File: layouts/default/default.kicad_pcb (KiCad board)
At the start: 2 copper layers, 37 x 37 mm, 107 parts

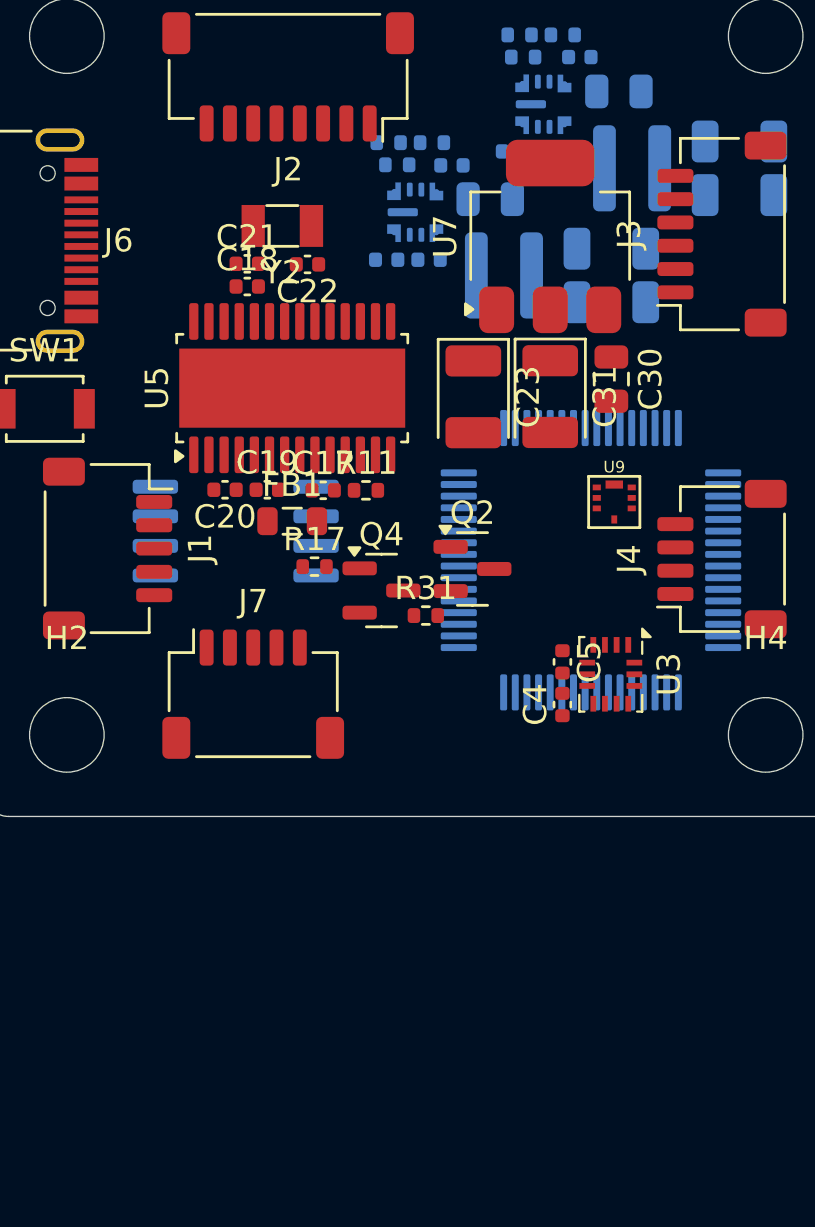
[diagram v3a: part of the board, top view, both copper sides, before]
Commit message: Replace AMS1117 with TI TLV75533 LDO, SS34 with SS54 Schottky
AMS1117 is Chinese (AMS, Shenzhen) — not NDAA compliant. TLV75533
is TI (SOT-23-5, 500mA, stable with MLCC). EN tied to VIN. SS54
is a drop-in 5A upgrade over SS34 (same SMA footprint). Both match
Brave F7 reference board components.

Co-Authored-By: Claude Opus 4.6 <noreply@anthropic.com>
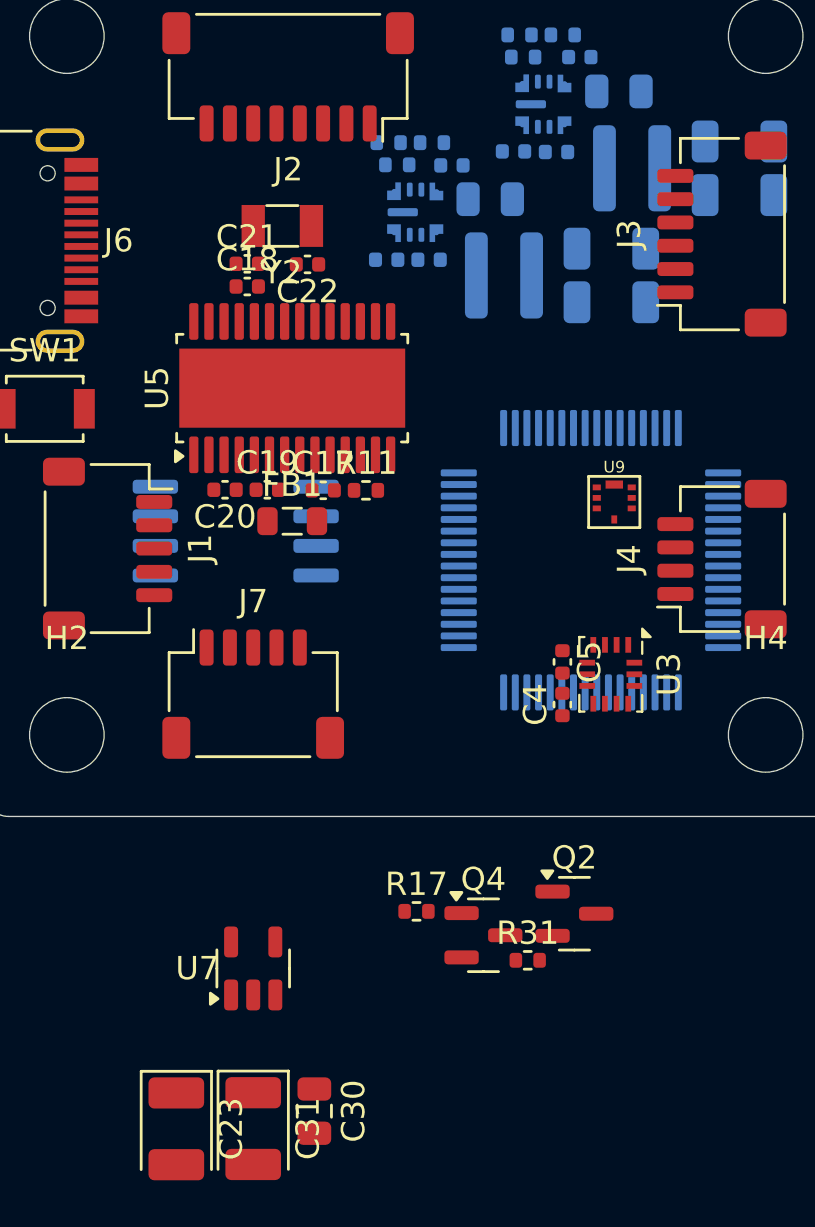
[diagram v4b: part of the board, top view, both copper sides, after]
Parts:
- U7: footprint Package_TO_SOT_SMD:SOT-223-3_TabPin2 -> Package_TO_SOT_SMD:SOT-23-5
- moved C30 33.9 mm to (114.1, 149.7)
- moved C31 33.9 mm to (111.5, 150.4)
- moved U7 33.9 mm to (111.5, 143.5)
- moved C23 33.9 mm to (108.2, 150.4)
- moved Q2 15.4 mm to (125.3, 141.2)
- moved R31 15.4 mm to (123.3, 143.2)
- moved Q4 15.4 mm to (121.4, 142.1)
- moved R17 15.4 mm to (118.5, 141.1)
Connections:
- U7 pad 1: baro-gnd -> v5
- U7 pad 2: vdd -> baro-gnd
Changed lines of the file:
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@@
     (footprint "Capacitor_Tantalum_SMD:CP_EIA-3528-21_Kemet-B"
         (layer "F.Cu")
-        (at 120.95 118.985 -90)
+        (at 108.2 150.41 -90)
         (property "Reference" "C23"
             (at 0 -2.35 90)
@@
     (footprint "Capacitor_SMD:C_0805_2012Metric"
         (layer "F.Cu")
-        (at 126.875 118.225 -90)
+        (at 114.125 149.65 -90)
         (property "Reference" "C30"
             (at 0 -1.68 90)
@@
     (footprint "Resistor_SMD:R_0402_1005Metric"
         (layer "F.Cu")
-        (at 118.91 128.375 0)
+        (at 123.285 143.175 0)
         (property "Reference" "R31"
             (at 0 -1.17 0)
@@
     (footprint "Package_TO_SOT_SMD:SOT-23"
         (layer "F.Cu")
-        (at 120.9125 126.375 0)
+        (at 125.2875 141.175 0)
         (property "Reference" "Q2"
             (at 0 -2.4 0)
@@
         )
     )
-    (footprint "Package_TO_SOT_SMD:SOT-223-3_TabPin2"
+    (footprint "Package_TO_SOT_SMD:SOT-23-5"
         (layer "F.Cu")
-        (at 124.25 112.1 90)
+        (at 111.5 143.525 90)
         (property "Reference" "U7"
-            (at 0 -4.5 90)
+            (at 0 -2.4 0)
             (layer "F.SilkS")
             (effects
@@
         )
         (property "Value" ""
-            (at 0 4.5 90)
+            (at 0 2.4 0)
             (layer "F.Fab")
             (hide no)
@@
             )
         )
-        (property "__atopile_lib_fp_hash__" "a6ccbecc-0be9-e1c9-66fc-8e409d184be7"
-            (at 0 0 90)
+        (property "__atopile_lib_fp_hash__" "1547344e-d8e7-4a11-2d2b-a920ed1ea8dd"
+            (at 0 0 0)
             (layer "User.9")
             (hide yes)
@@
         (attr smd)
         (fp_line
-            (start 1.91 -3.41)
-            (end 1.91 -2.15)
+            (start 0 -1.56)
+            (end -0.8 -1.56)
             (stroke
                 (width 0.12)
@@
         )
         (fp_line
-            (start -1.85 -3.41)
-            (end 1.91 -3.41)
+            (start 0 -1.56)
+            (end 0.8 -1.56)
             (stroke
                 (width 0.12)
@@
         )
         (fp_line
-            (start 1.91 3.41)
-            (end 1.91 2.15)
+            (start 0 1.56)
+            (end -0.8 1.56)
             (stroke
                 (width 0.12)
@@
         )
         (fp_line
-            (start -1.85 3.41)
-            (end 1.91 3.41)
+            (start 0 1.56)
+            (end 0.8 1.56)
             (stroke
                 (width 0.12)
@@
         )
         (fp_line
-            (start 4.4 -3.6)
-            (end -4.4 -3.6)
+            (start -2.05 -1.5)
+            (end -1.05 -1.5)
             (stroke
                 (width 0.05)
@@
         )
         (fp_line
-            (start -4.4 -3.6)
-            (end -4.4 3.6)
+            (start -2.05 1.5)
+            (end -2.05 -1.5)
             (stroke
                 (width 0.05)
@@
         )
         (fp_line
-            (start 4.4 3.6)
-            (end 4.4 -3.6)
+            (start -1.05 -1.7)
+            (end 1.05 -1.7)
             (stroke
                 (width 0.05)
@@
         )
         (fp_line
-            (start -4.4 3.6)
-            (end 4.4 3.6)
+            (start -1.05 -1.5)
+            (end -1.05 -1.7)
             (stroke
                 (width 0.05)
@@
         )
         (fp_line
-            (start 1.85 -3.35)
-            (end 1.85 3.35)
+            (start -1.05 1.5)
+            (end -2.05 1.5)
             (stroke
-                (width 0.1)
+                (width 0.05)
                 (type solid)
             )
-            (layer "F.Fab")
+            (layer "F.CrtYd")
         )
         (fp_line
-            (start -0.85 -3.35)
-            (end 1.85 -3.35)
+            (start -1.05 1.7)
+            (end -1.05 1.5)
             (stroke
-                (width 0.1)
+                (width 0.05)
                 (type solid)
             )
-            (layer "F.Fab")
+            (layer "F.CrtYd")
         )
         (fp_line
-            (start -1.85 -2.35)
-            (end -0.85 -3.35)
+            (start 1.05 -1.7)
+            (end 1.05 -1.5)
             (stroke
-                (width 0.1)
+                (width 0.05)
                 (type solid)
             )
-            (layer "F.Fab")
+            (layer "F.CrtYd")
         )
         (fp_line
-            (start -1.85 -2.35)
-            (end -1.85 3.35)
+            (start 1.05 -1.5)
+            (end 2.05 -1.5)
             (stroke
-                (width 0.1)
+                (width 0.05)
                 (type solid)
             )
-            (layer "F.Fab")
+            (layer "F.CrtYd")
+        )
+        (fp_line
+            (start 1.05 1.5)
+            (end 1.05 1.7)
+            (stroke
+                (width 0.05)
+                (type solid)
+            )
+            (layer "F.CrtYd")
         )
         (fp_line
-            (start -1.85 3.35)
-            (end 1.85 3.35)
+            (start 1.05 1.7)
+            (end -1.05 1.7)
             (stroke
-                (width 0.1)
+                (width 0.05)
                 (type solid)
             )
+            (layer "F.CrtYd")
+        )
+        (fp_line
+            (start 2.05 -1.5)
+            (end 2.05 1.5)
+            (stroke
+                (width 0.05)
+                (type solid)
+            )
+            (layer "F.CrtYd")
+        )
+        (fp_line
+            (start 2.05 1.5)
+            (end 1.05 1.5)
+            (stroke
+                (width 0.05)
+                (type solid)
+            )
+            (layer "F.CrtYd")
+        )
+        (fp_text user "${REFERENCE}"
+            (at 0 0 0)
             (layer "F.Fab")
+            (effects
+                (font
+                    (size 0.4 0.4)
+                    (thickness 0.06)
+                )
+                (hide yes)
+            )
+            (unlocked no)
         )
         (fp_poly
             (pts
-                (xy -3.13 -3.31)
-                (xy -3.37 -3.64)
-                (xy -2.89 -3.64)
-                (xy -3.13 -3.31)
+                (xy -1.3 -1.51)
+                (xy -1.54 -1.84)
+                (xy -1.06 -1.84)
             )
             (stroke
@@
             (layer "F.SilkS")
         )
+        (fp_poly
+            (pts
+                (xy -0.8 -1.05)
+                (xy -0.8 1.45)
+                (xy 0.8 1.45)
+                (xy 0.8 -1.45)
+                (xy -0.4 -1.45)
+            )
+            (stroke
+                (width 0.1)
+                (type solid)
+            )
+            (fill no)
+            (layer "F.Fab")
+        )
         (pad "1" smd roundrect
-            (at -3.15 -2.3 90)
-            (size 2 1.5)
+            (at -1.1375 -0.95 90)
+            (size 1.325 0.6)
             (layers "F.Cu" "F.Mask" "F.Paste")
             (roundrect_rratio 0.25)
-            (net 41 "baro-gnd")
+            (net 50 "v5")
         )
         (pad "2" smd roundrect
-            (at -3.15 0 90)
-            (size 2 1.5)
+            (at -1.1375 0 90)
+            (size 1.325 0.6)
             (layers "F.Cu" "F.Mask" "F.Paste")
             (roundrect_rratio 0.25)
-            (net 65 "vdd")
+            (net 41 "baro-gnd")
         )
-        (pad "2" smd roundrect
-            (at 3.15 0 90)
-            (size 2 3.8)
+        (pad "3" smd roundrect
+            (at -1.1375 0.95 90)
+            (size 1.325 0.6)
             (layers "F.Cu" "F.Mask" "F.Paste")
             (roundrect_rratio 0.25)
-            (net 65 "vdd")
+            (net 50 "v5")
         )
-        (pad "3" smd roundrect
-            (at -3.15 2.3 90)
-            (size 2 1.5)
+        (pad "4" smd roundrect
+            (at 1.1375 0.95 90)
+            (size 1.325 0.6)
             (layers "F.Cu" "F.Mask" "F.Paste")
             (roundrect_rratio 0.25)
-            (net 50 "v5")
+        )
+        (pad "5" smd roundrect
+            (at 1.1375 -0.95 90)
+            (size 1.325 0.6)
+            (layers "F.Cu" "F.Mask" "F.Paste")
+            (roundrect_rratio 0.25)
+            (net 65 "vdd")
         )
         (embedded_fonts no)
-        (model "${KICAD9_3DMODEL_DIR}/Package_TO_SOT_SMD.3dshapes/SOT-223.step"
+        (model "${KICAD9_3DMODEL_DIR}/Package_TO_SOT_SMD.3dshapes/SOT-23-5.step"
             (offset
                 (xyz 0 0 0)
@@
     (footprint "Package_TO_SOT_SMD:SOT-23"
         (layer "F.Cu")
-        (at 117.0075 127.3 0)
+        (at 121.3825 142.1 0)
         (property "Reference" "Q4"
             (at 0 -2.4 0)
@@
     (footprint "Resistor_SMD:R_0402_1005Metric"
         (layer "F.Cu")
-        (at 114.135 126.275 0)
+        (at 118.51 141.075 0)
         (property "Reference" "R17"
             (at 0 -1.17 0)
@@
     (footprint "Capacitor_Tantalum_SMD:CP_EIA-3528-21_Kemet-B"
         (layer "F.Cu")
-        (at 124.25 118.975 -90)
+        (at 111.5 150.4 -90)
         (property "Reference" "C31"
             (at 0 -2.35 90)

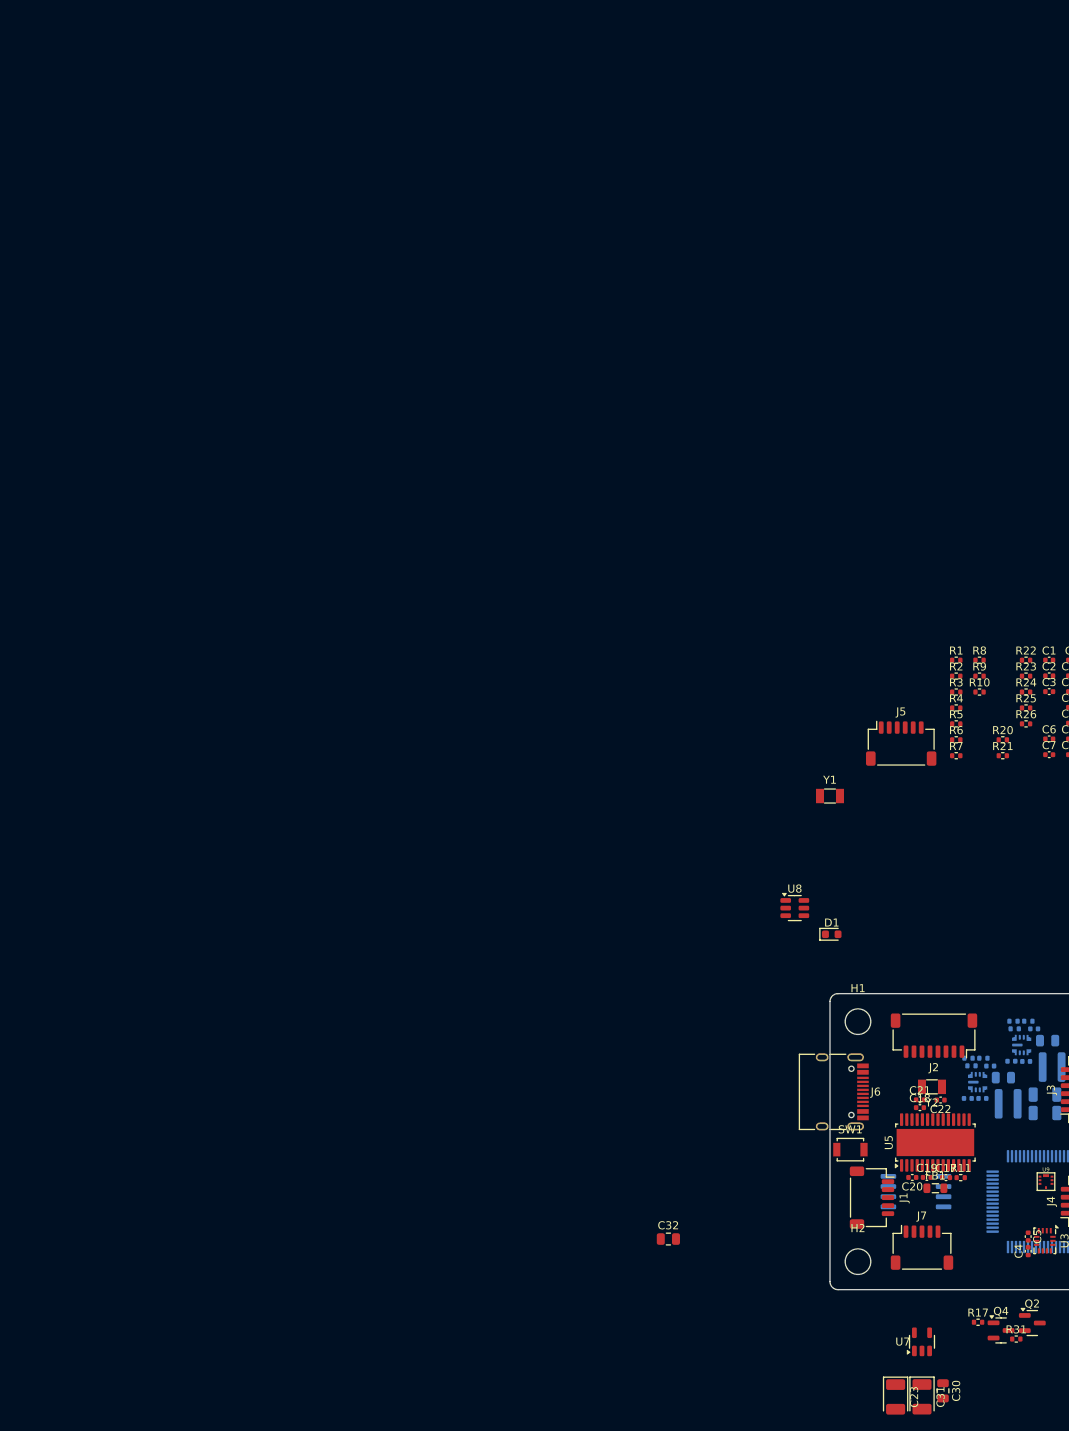
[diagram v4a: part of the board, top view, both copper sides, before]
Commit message: Revert VTX BEC from fixed 5V to adjustable 10V (REV-010)
Brave F7 reference outputs 10V on its VTX connector, not 5V.
VTX buck changed from LMR43620MB5RPER (fixed) to LMR43620RNXTRPER
(adjustable) with 13kΩ RT resistor and 90.9kΩ/10kΩ FB divider
for 10.09V output. PINIO1 P-FET switch updated for 10V rail.

Co-Authored-By: Claude Opus 4.6 <noreply@anthropic.com>
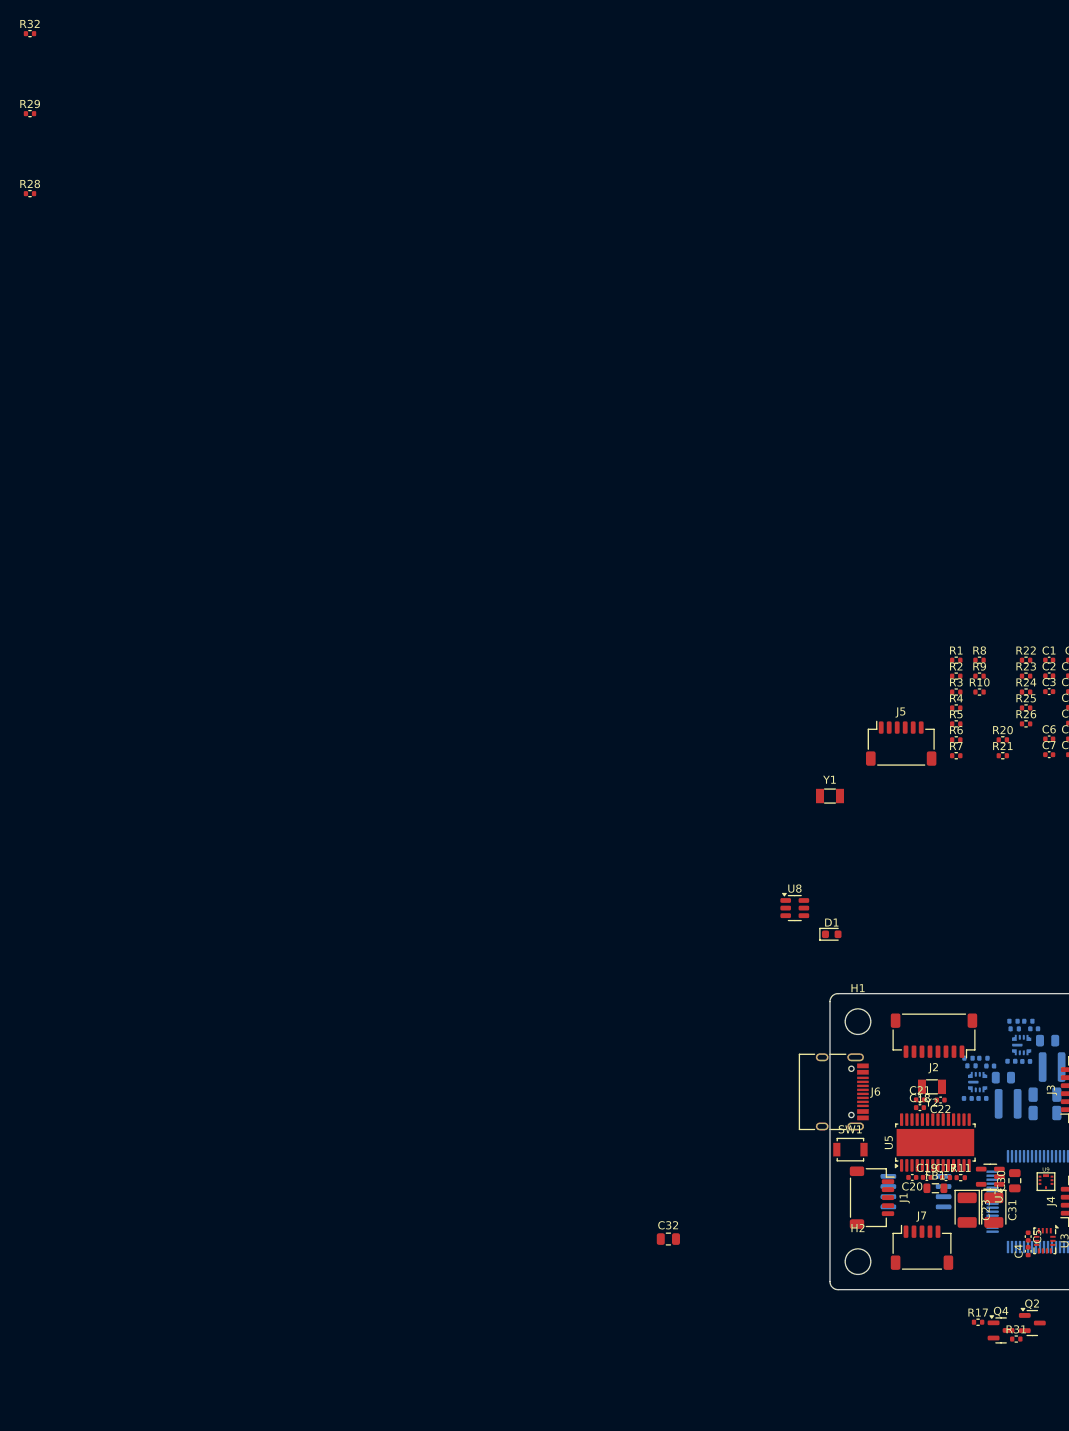
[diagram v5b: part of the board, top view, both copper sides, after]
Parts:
- added R28: , Resistor_SMD:R_0402_1005Metric, F.Cu at (0.00, 0.00)
- added R29: , Resistor_SMD:R_0402_1005Metric, F.Cu at (0.00, -10.0)
- added R32: , Resistor_SMD:R_0402_1005Metric, F.Cu at (0.00, -20.0)
- moved C30 27.8 mm to (123.1, 123.4), turned to 90 degrees
- moved C23 25.0 mm to (117.2, 127.1)
- moved C31 25.0 mm to (120.5, 127.1)
- moved U7 22.3 mm to (120.0, 122.9), turned to 180 degrees
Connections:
- net vtx_5v renamed vtx_10v
- C37 pad 1: rail_5v_vtx -> rail_10v_vtx
- C38 pad 1: rail_5v_vtx -> rail_10v_vtx
- L2 pad 2: rail_5v_vtx -> rail_10v_vtx
- Q2 pad 2: rail_5v_vtx -> rail_10v_vtx
- R15 pad 2: rail_5v_vtx -> rail_10v_vtx
- R31 pad 2: rail_5v_vtx -> rail_10v_vtx
- U1 pad 1: baro-gnd -> rt
- U1 pad 8: rail_5v_vtx -> fb
